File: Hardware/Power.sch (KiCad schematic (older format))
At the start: 20 parts, among them U601 PAM2306AYPAA, U602 MIC5317-2.5YM5

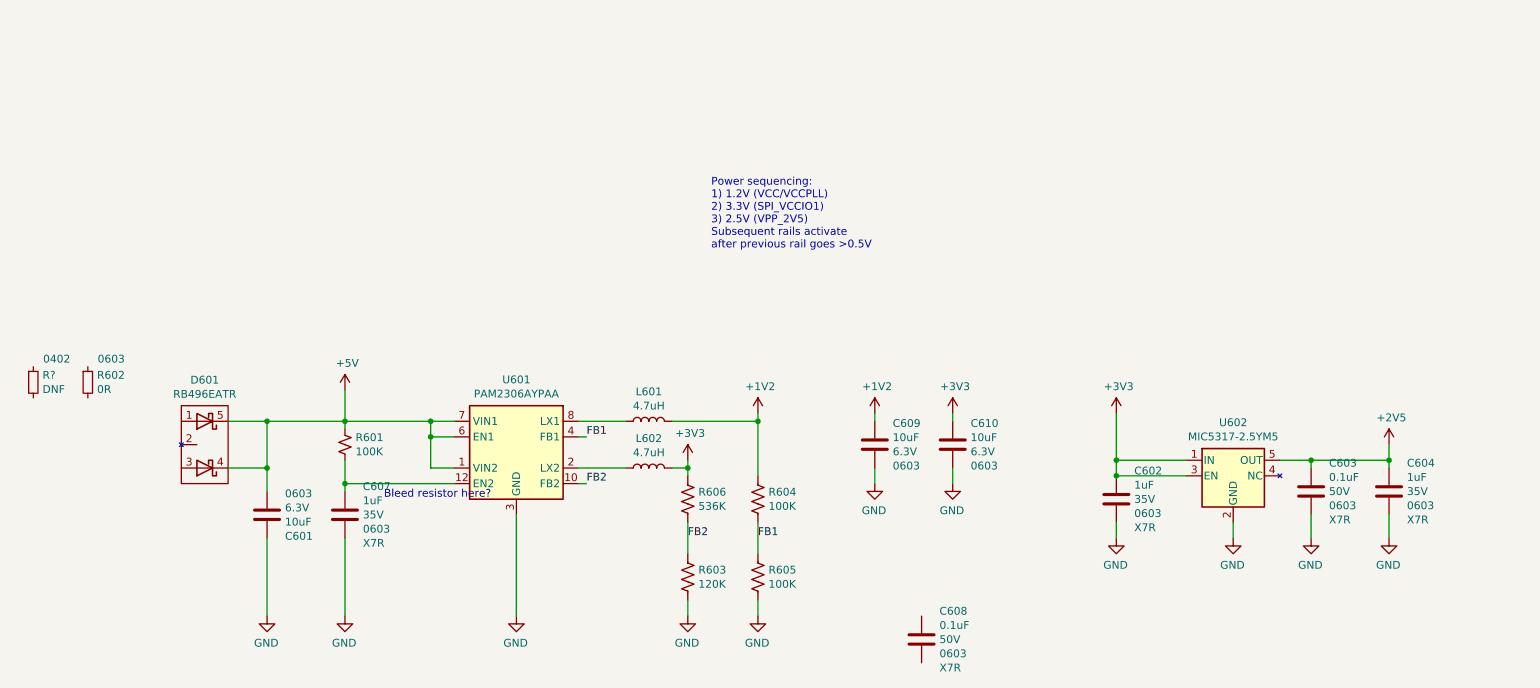
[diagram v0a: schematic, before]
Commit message: More passives.
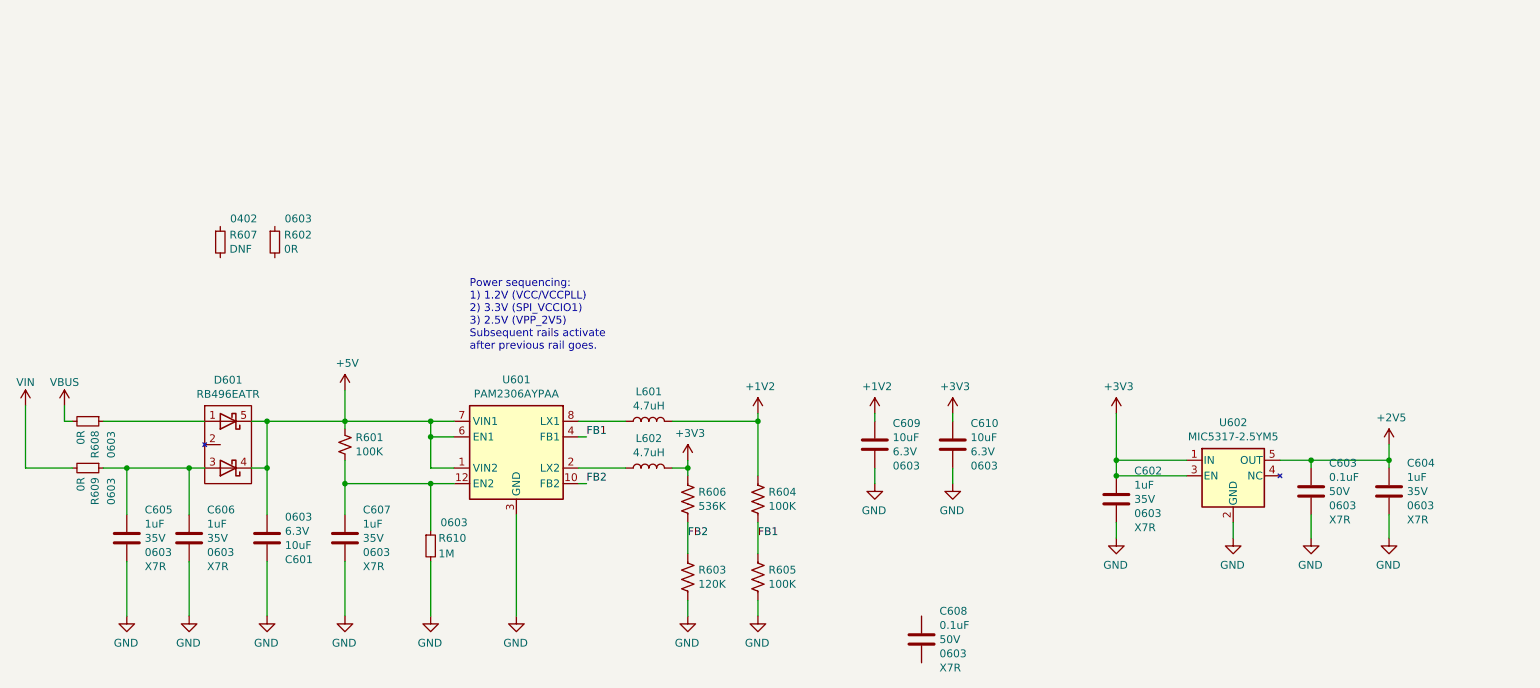
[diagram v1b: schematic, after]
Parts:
- added C605, C606: 1uF, Capacitor_SMD:C_0603_1608Metric, symbol Device:C
- added R608, R609: 0R, Resistor_SMD:R_0603_1608Metric, symbol Device:R_Small
- added R610: 1M, Resistor_SMD:R_0603_1608Metric, symbol Device:R_Small
- gave numbers to parts that had none: 1
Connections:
- net GND: now also C605.2, C606.2, R610.2
- net at C607.1, R601.2, U601.12 (EN2): now also R610.1
- net at D601.1 (A1): now also R608.1
- net at D601.3 (A2): now also C605.1, C606.1, R609.1
- new net VBUS: R608.2
- new net VIN: R609.2
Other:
- note added: "Power sequencing:\n1) 1.2V (VCC/VCCPLL)\n2) 3.3V (SPI_VCCIO1)\n3) 2.5V (VPP_2V5)\nSubsequent rails activate\nafter previous rail goes."
- note removed: "Bleed resistor here?"
- note removed: "Power sequencing:\n1) 1.2V (VCC/VCCPLL)\n2) 3.3V (SPI_VCCIO1)\n3) 2.5V (VPP_2V5)\nSubsequent rails activate\nafter previous rail goes >0.5V"
- moved on the sheet: C601, C607, D601, R602, R607

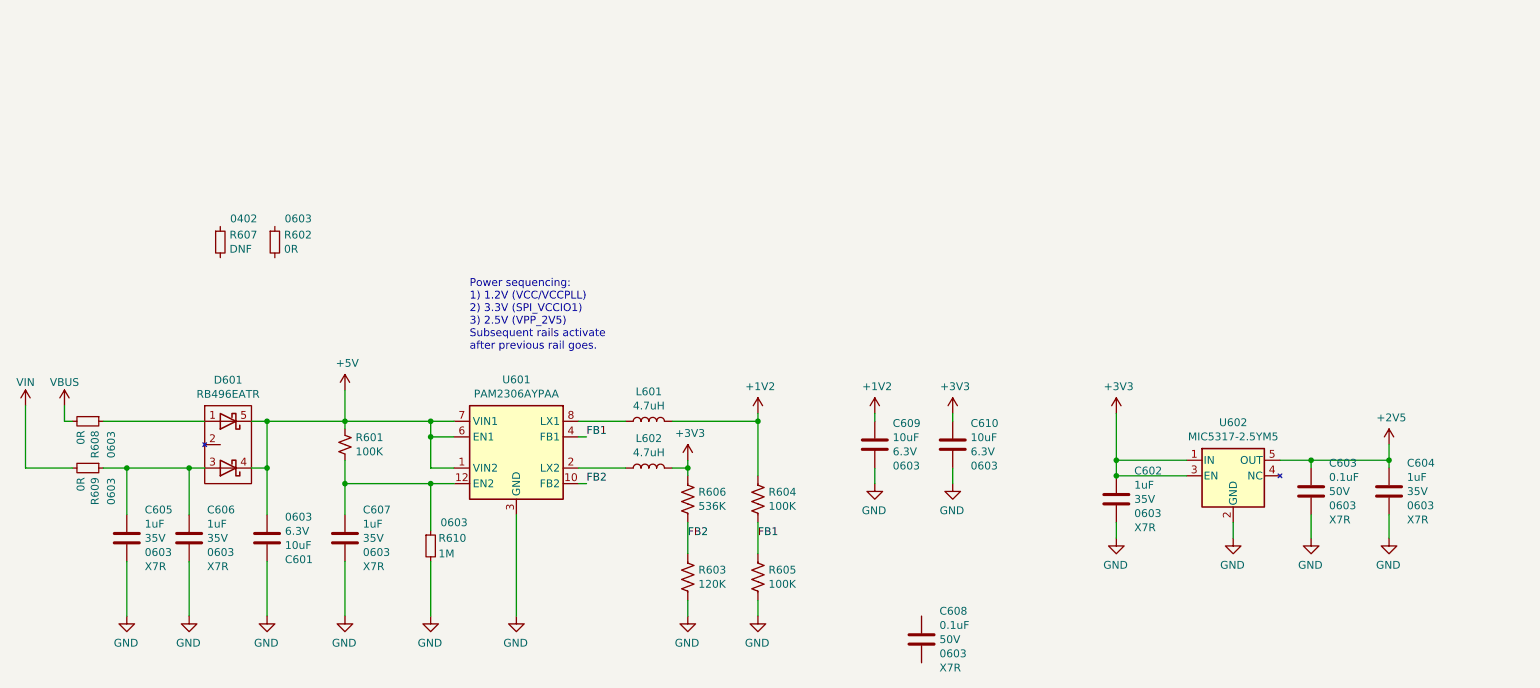
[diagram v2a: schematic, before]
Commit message: Think this is close to fixing the power circuitry.
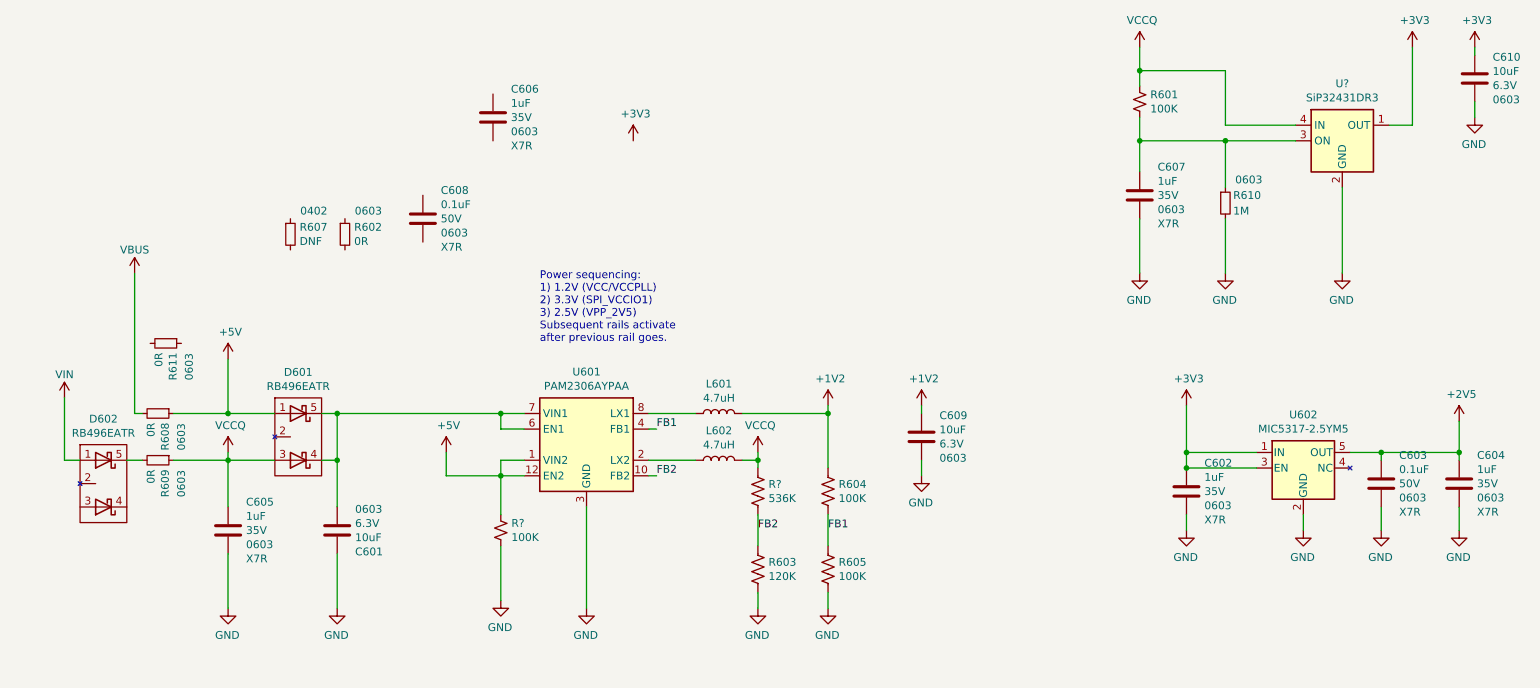
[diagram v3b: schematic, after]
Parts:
- removed R606: 536K, Resistor_SMD:R_0603_1608Metric, symbol Device:R_US
- added D602: RB496EATR, Package_TO_SOT_SMD:SOT-23-5, symbol OHMC2022:RB496EATR
- added R611: 0R, Resistor_SMD:R_0603_1608Metric, symbol Device:R_Small
- added R?: 536K, Resistor_SMD:R_0603_1608Metric, symbol Device:R_US
- added R?: 100K, Resistor_SMD:R_0603_1608Metric, symbol Device:R_Small_US
- added U?: SiP32431DR3, Package_TO_SOT_SMD:SOT-363_SC-70-6, symbol Power_Management:SiP32431DR3
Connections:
- net +3V3: now also U?.1 (OUT); no longer L602.2
- net +5V: now also D601.1 (A1), R608.1, U601.12 (EN2), R?.1; no longer C601.2, D601.4 (K2), D601.5 (K1), R601.1, U601.6 (EN1), U601.7 (VIN1)
- net FB2: now also R?.2
- net GND: now also R?.2, U?.2 (GND), U?.5 (GND); no longer C606.2
- net VIN: now also D602.1 (A1); no longer R609.2
- net at C607.1, R601.2, R610.1: now also U?.3 (ON); no longer U601.12 (EN2)
- net VCCQ: now reaches C605.1, D601.3 (A2), R609.1
- net VCCQ: now also L602.2, R601.1, R?.1, U?.4 (IN); no longer C606.1
- new net: C601.2, D601.4 (K2), D601.5 (K1), U601.6 (EN1), U601.7 (VIN1)
- new net: D602.5 (K1), R609.2
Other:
- moved on the sheet: C601, C602, C603, C604, C605, C606, C607, C608, C609, C610, D601, L601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

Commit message: Commit berfore merge back with power fix.
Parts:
- removed C606: 1uF, Capacitor_SMD:C_0603_1608Metric, symbol Device:C
- removed C608: 0.1uF, Capacitor_SMD:C_0603_1608Metric, symbol Device:C
- removed R602, R611: 0R, Resistor_SMD:R_0603_1608Metric, symbol Device:R_Small
- removed R607: DNF, Resistor_SMD:R_0402_1005Metric, symbol Device:R_Small
- U603: renamed from U?; DPN (none) -> SIP32431DR3-T1GE3CT-ND; MPN (none) -> SIP32431DR3-T1GE3
- gave numbers to parts that had none: 2
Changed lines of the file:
@@
-$EndComp
-$Comp
-L Device:C C608
-U 1 1 612DD1F9
-P 3150 2300
-F 0 "C608" H 3265 2482 50  0000 L CNN
-F 1 "0.1uF" H 3265 2391 50  0000 L CNN
-F 2 "Capacitor_SMD:C_0603_1608Metric" H 3188 2150 50  0001 C CNN
-F 3 "~" H 3150 2300 50  0001 C CNN
-F 4 "C0603C104K5RACAUTO" H 3150 2300 50  0001 C CNN "MPN"
-F 5 "399-6856-1-ND" H 3150 2300 50  0001 C CNN "DPN"
-F 6 "50V" H 3265 2300 50  0000 L CNN "Tol"
-F 7 "0603" H 3265 2209 50  0000 L CNN "Pkg"
-F 8 "X7R" H 3265 2118 50  0000 L CNN "TCoff"
-	1    3150 2300
-	1    0    0    -1
 $EndComp
 $Comp
@@
 F 3 "" H 1900 3200 50  0001 C CNN
 	1    1900 3200
-	1    0    0    -1
-$EndComp
-$Comp
-L Device:R_Small R602
-U 1 1 612F9833
-P 2650 2400
-F 0 "R602" H 2709 2446 50  0000 L CNN
-F 1 "0R" H 2709 2355 50  0000 L CNN
-F 2 "Resistor_SMD:R_0603_1608Metric" V 2580 2400 50  0001 C CNN
-F 3 "~" H 2650 2400 50  0001 C CNN
-F 4 "0603" H 2800 2550 50  0000 C CNN "Pkg"
-F 5 "RC0603JR-070RL" H 2650 2400 50  0001 C CNN "MPN"
-F 6 "311-0.0GRCT-ND" H 2650 2400 50  0001 C CNN "DPN"
-	1    2650 2400
 	1    0    0    -1
 $EndComp
@@
 	2600 4450 2600 4800
 $Comp
-L Device:R_Small R607
-U 1 1 6147B8D3
-P 2300 2400
-F 0 "R607" H 2359 2446 50  0000 L CNN
-F 1 "DNF" H 2359 2355 50  0000 L CNN
-F 2 "Resistor_SMD:R_0402_1005Metric" V 2230 2400 50  0001 C CNN
-F 3 "~" H 2300 2400 50  0001 C CNN
-F 4 "0402" H 2450 2550 50  0000 C CNN "Pkg"
-F 5 "" H 2300 2400 50  0001 C CNN "MPN"
-F 6 "" H 2300 2400 50  0001 C CNN "DPN"
-	1    2300 2400
-	1    0    0    -1
-$EndComp
-$Comp
 L power:VBUS #PWR?
 U 1 1 614E2688
@@
 Wire Wire Line
 	1900 3850 1900 4150
-$Comp
-L Device:C C606
-U 1 1 614F14AF
-P 3600 1650
-F 0 "C606" H 3715 1832 50  0000 L CNN
-F 1 "1uF" H 3715 1741 50  0000 L CNN
-F 2 "Capacitor_SMD:C_0603_1608Metric" H 3638 1500 50  0001 C CNN
-F 3 "~" H 3600 1650 50  0001 C CNN
-F 4 "GMK107AB7105KAHT" H 3600 1650 50  0001 C CNN "MPN"
-F 5 "587-3352-1-ND" H 3600 1650 50  0001 C CNN "DPN"
-F 6 "35V" H 3715 1650 50  0000 L CNN "Tol"
-F 7 "0603" H 3715 1559 50  0000 L CNN "Pkg"
-F 8 "X7R" H 3715 1468 50  0000 L CNN "TCoff"
-	1    3600 1650
-	1    0    0    -1
-$EndComp
 $Comp
 L Device:C C605
@@
 Wire Wire Line
 	1250 3850 1350 3850
-$Comp
-L Device:R_Small R611
-U 1 1 6153EF6E
-P 1500 3100
-F 0 "R611" H 1559 3146 50  0000 L CNN
-F 1 "0R" H 1559 3055 50  0000 L CNN
-F 2 "Resistor_SMD:R_0603_1608Metric" V 1430 3100 50  0001 C CNN
-F 3 "~" H 1500 3100 50  0001 C CNN
-F 4 "0603" H 1650 3250 50  0000 C CNN "Pkg"
-F 5 "RC0603JR-070RL" H 1500 3100 50  0001 C CNN "MPN"
-F 6 "311-0.0GRCT-ND" H 1500 3100 50  0001 C CNN "DPN"
-	1    1500 3100
-	0    1    1    0
-$EndComp
 Wire Wire Line
 	4200 4150 4200 4800
@@
 	3650 3950 3300 3950
 Connection ~ 3650 3950
-$Comp
-L power:+3V3 #PWR?
-U 1 1 6159D3FF
-P 4500 1800
-AR Path="/6123BB15/6159D3FF" Ref="#PWR?"  Part="1"
-AR Path="/611E335F/6159D3FF" Ref="#PWR0146"  Part="1"
-F 0 "#PWR0146" H 4500 1650 50  0001 C CNN
-F 1 "+3V3" H 4515 1973 50  0000 C CNN
-F 2 "" H 4500 1800 50  0001 C CNN
-F 3 "" H 4500 1800 50  0001 C CNN
-	1    4500 1800
-	1    0    0    -1
-$EndComp
 Wire Wire Line
 	1900 3800 1900 3850
 Connection ~ 1900 3850
 $Comp
-L Power_Management:SiP32431DR3 U?
+L Power_Management:SiP32431DR3 U603
 U 1 1 615CC64C
 P 9050 1800
-F 0 "U?" H 9050 2167 50  0000 C CNN
+F 0 "U603" H 9050 2167 50  0000 C CNN
 F 1 "SiP32431DR3" H 9050 2076 50  0000 C CNN
 F 2 "Package_TO_SOT_SMD:SOT-363_SC-70-6" H 9050 2250 50  0001 C CNN
 F 3 "https://www.vishay.com/docs/66597/sip32431.pdf" H 9050 1800 50  0001 C CNN
+F 4 "SIP32431DR3-T1GE3" H 9050 1800 50  0001 C CNN "MPN"
+F 5 "SIP32431DR3-T1GE3CT-ND" H 9050 1800 50  0001 C CNN "DPN"
 	1    9050 1800
 	1    0    0    -1
@@
 	1900 3850 2200 3850
 $Comp
-L power:VCCQ #PWR?
+L power:VCCQ #PWR0127
 U 1 1 6163B082
 P 1900 3800
-F 0 "#PWR?" H 1900 3650 50  0001 C CNN
+F 0 "#PWR0127" H 1900 3650 50  0001 C CNN
 F 1 "VCCQ" H 1915 3973 50  0000 C CNN
 F 2 "" H 1900 3800 50  0001 C CNN
@@
 $EndComp
 $Comp
-L power:VCCQ #PWR?
+L power:VCCQ #PWR0133
 U 1 1 6163B616
 P 7750 1200
-F 0 "#PWR?" H 7750 1050 50  0001 C CNN
+F 0 "#PWR0133" H 7750 1050 50  0001 C CNN
 F 1 "VCCQ" H 7765 1373 50  0000 C CNN
 F 2 "" H 7750 1200 50  0001 C CNN
@@
 P 9800 3600
 AR Path="/6123BB15/61643B95" Ref="#PWR?"  Part="1"
-AR Path="/611E335F/61643B95" Ref="#PWR?"  Part="1"
-F 0 "#PWR?" H 9800 3450 50  0001 C CNN
+AR Path="/611E335F/61643B95" Ref="#PWR0144"  Part="1"
+F 0 "#PWR0144" H 9800 3450 50  0001 C CNN
 F 1 "+2V5" H 9815 3773 50  0000 C CNN
 F 2 "" H 9800 3600 50  0001 C CNN
@@
 	9800 3600 9800 3800
 $Comp
-L Device:R_US R?
+L Device:R_US R612
 U 1 1 61646B47
 P 5300 4050
-F 0 "R?" H 5368 4096 50  0000 L CNN
+F 0 "R612" H 5368 4096 50  0000 L CNN
 F 1 "536K" H 5368 4005 50  0000 L CNN
 F 2 "Resistor_SMD:R_0603_1608Metric" V 5230 4050 50  0001 C CNN
@@
 $EndComp
 $Comp
-L power:VCCQ #PWR?
+L power:VCCQ #PWR0145
 U 1 1 61647105
 P 5300 3800
-F 0 "#PWR?" H 5300 3650 50  0001 C CNN
+F 0 "#PWR0145" H 5300 3650 50  0001 C CNN
 F 1 "VCCQ" H 5315 3973 50  0000 C CNN
 F 2 "" H 5300 3800 50  0001 C CNN
@@
 P 3300 3800
 AR Path="/6123BB15/61649A7A" Ref="#PWR?"  Part="1"
-AR Path="/611E335F/61649A7A" Ref="#PWR?"  Part="1"
-F 0 "#PWR?" H 3300 3650 50  0001 C CNN
+AR Path="/611E335F/61649A7A" Ref="#PWR0146"  Part="1"
+F 0 "#PWR0146" H 3300 3650 50  0001 C CNN
 F 1 "+5V" H 3315 3973 50  0000 C CNN
 F 2 "" H 3300 3800 50  0001 C CNN
@@
 P 9050 2650
 AR Path="/611E3335/61660820" Ref="#PWR?"  Part="1"
-AR Path="/611E335F/61660820" Ref="#PWR?"  Part="1"
-F 0 "#PWR?" H 9050 2400 50  0001 C CNN
+AR Path="/611E335F/61660820" Ref="#PWR0147"  Part="1"
+F 0 "#PWR0147" H 9050 2400 50  0001 C CNN
 F 1 "GND" H 9055 2477 50  0000 C CNN
 F 2 "" H 9050 2650 50  0001 C CNN
@@
 	1900 3550 2200 3550
 $Comp
-L Device:R_Small_US R?
+L Device:R_Small_US R606
 U 1 1 61667848
 P 3650 4300
-F 0 "R?" H 3718 4346 50  0000 L CNN
+F 0 "R606" H 3718 4346 50  0000 L CNN
 F 1 "100K" H 3718 4255 50  0000 L CNN
 F 2 "Resistor_SMD:R_0603_1608Metric" V 3580 4300 50  0001 C CNN
@@
 P 3650 4750
 AR Path="/611E3335/6166F420" Ref="#PWR?"  Part="1"
-AR Path="/611E335F/6166F420" Ref="#PWR?"  Part="1"
-F 0 "#PWR?" H 3650 4500 50  0001 C CNN
+AR Path="/611E335F/6166F420" Ref="#PWR0178"  Part="1"
+F 0 "#PWR0178" H 3650 4500 50  0001 C CNN
 F 1 "GND" H 3655 4577 50  0000 C CNN
 F 2 "" H 3650 4750 50  0001 C CNN
